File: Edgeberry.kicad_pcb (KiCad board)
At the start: 2 copper layers, 135 x 90 mm, 161 parts, among them P1 12Vin, Q1 BC547, Q2 BC547, Q3 BC547, SW1 SW_PUSH, U1 24LC256, U2 LM2596S-5.0

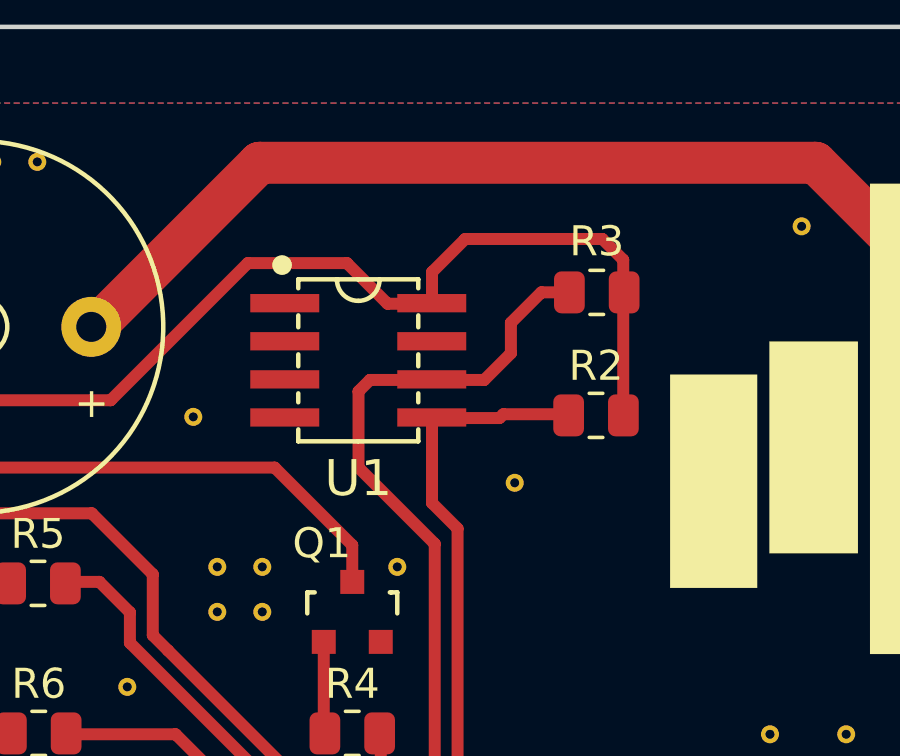
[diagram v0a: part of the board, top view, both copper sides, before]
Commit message: EEPROM write protection circuit + update version to 1.3
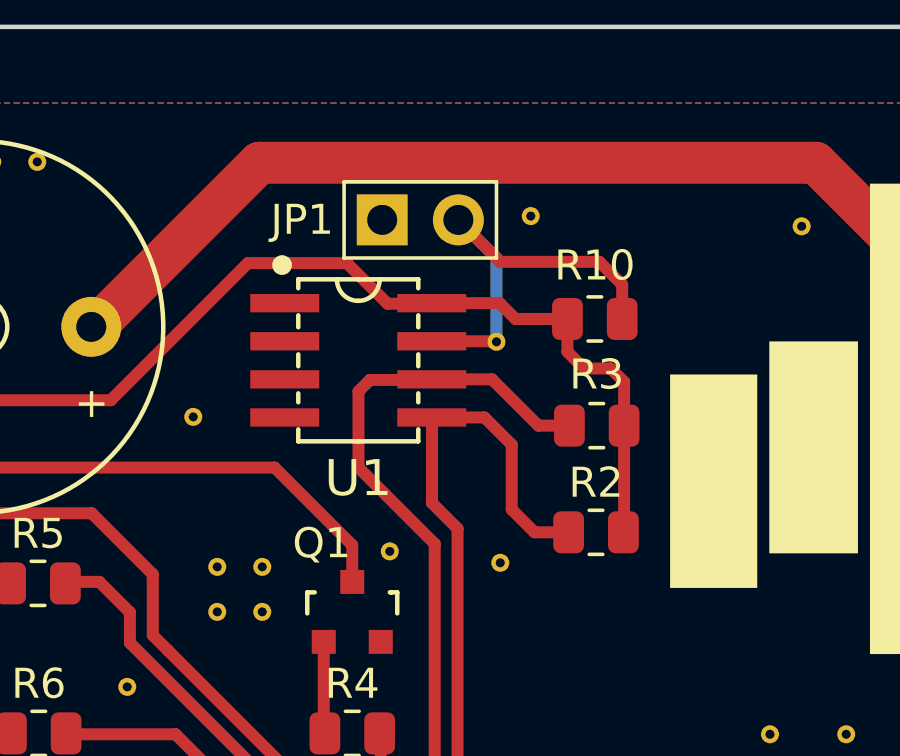
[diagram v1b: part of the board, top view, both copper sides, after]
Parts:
- added ?: , , F.Cu at (125.0, 62.3)
- added ?: , , F.Cu at (126.1, 58.1)
- added JP1: Jumper_2_Open, Connector_PinHeader_2.54mm:PinHeader_1x02_P2.54mm_Vertical, F.Cu at (121.1, 58.2)
- added R10: 10k, Resistor_SMD:R_0805_2012Metric, F.Cu at (128.2, 61.5)
- C1, C2: value 220uF -> 330uF
- moved R3 4.44 mm to (128.3, 65.1)
- moved R2 3.90 mm to (128.3, 68.6), turned to 180 degrees
- moved REF** 2.71 mm to (125.1, 69.6)
- moved REF** 0.57 mm to (121.4, 69.3)
- moved G*** 0.15 mm to (148.7, 63.3)
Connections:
- R2 pad 1: ID_SDA -> +3V3
- R2 pad 2: +3V3 -> ID_SDA
- REF** pad 1: (no net) -> GND
- U1 pad 7: GND -> WP
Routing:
- net WP: track 0.00 -> 14.3 mm
- net ID_SDA: track 29.0 -> 31.9 mm
- net ID_SCL: track 31.4 -> 30.4 mm
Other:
- board text added: "REV 1.3"
- board text added: "REV.: 1.3, Mid 2024"
- board text removed: "REV 1.2"
- board text removed: "REV.: 1.2, Mid 2024"

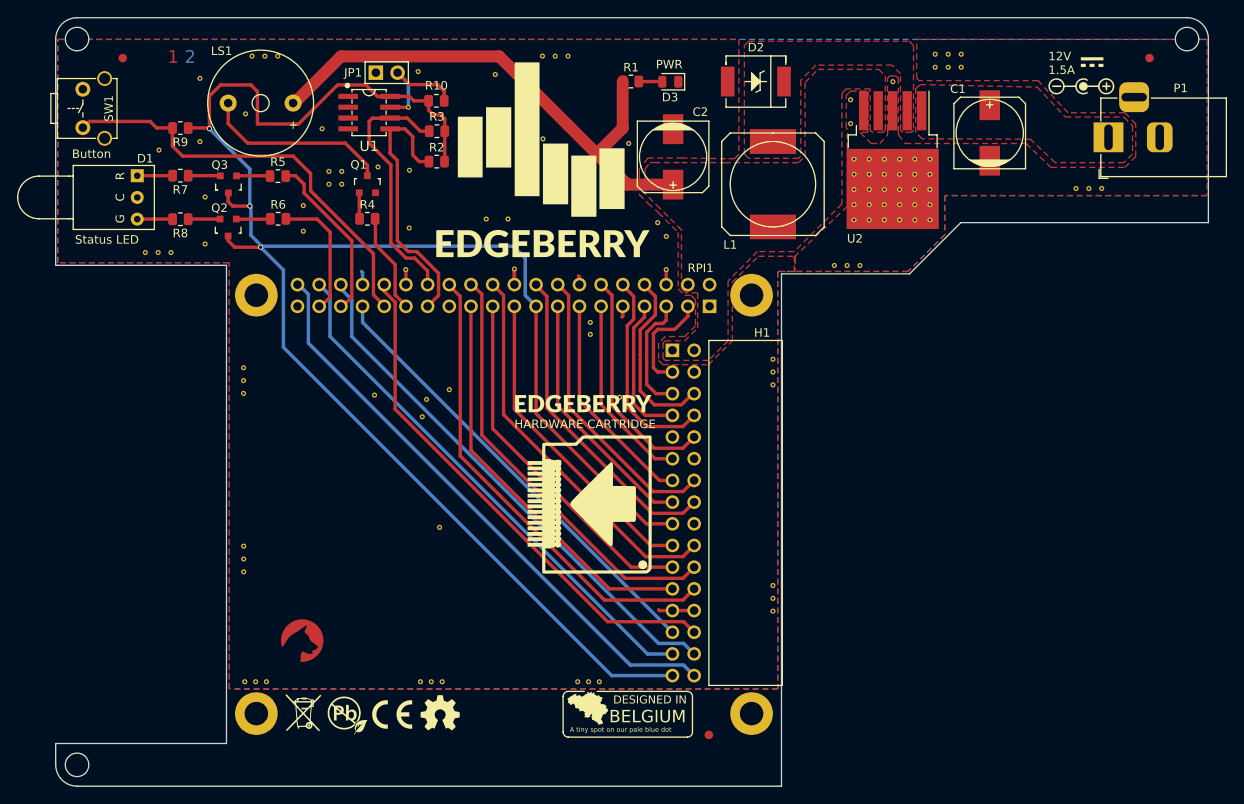
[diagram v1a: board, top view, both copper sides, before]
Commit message: Status LED on 5V instead of 3V3 + silkscreen aesthetics
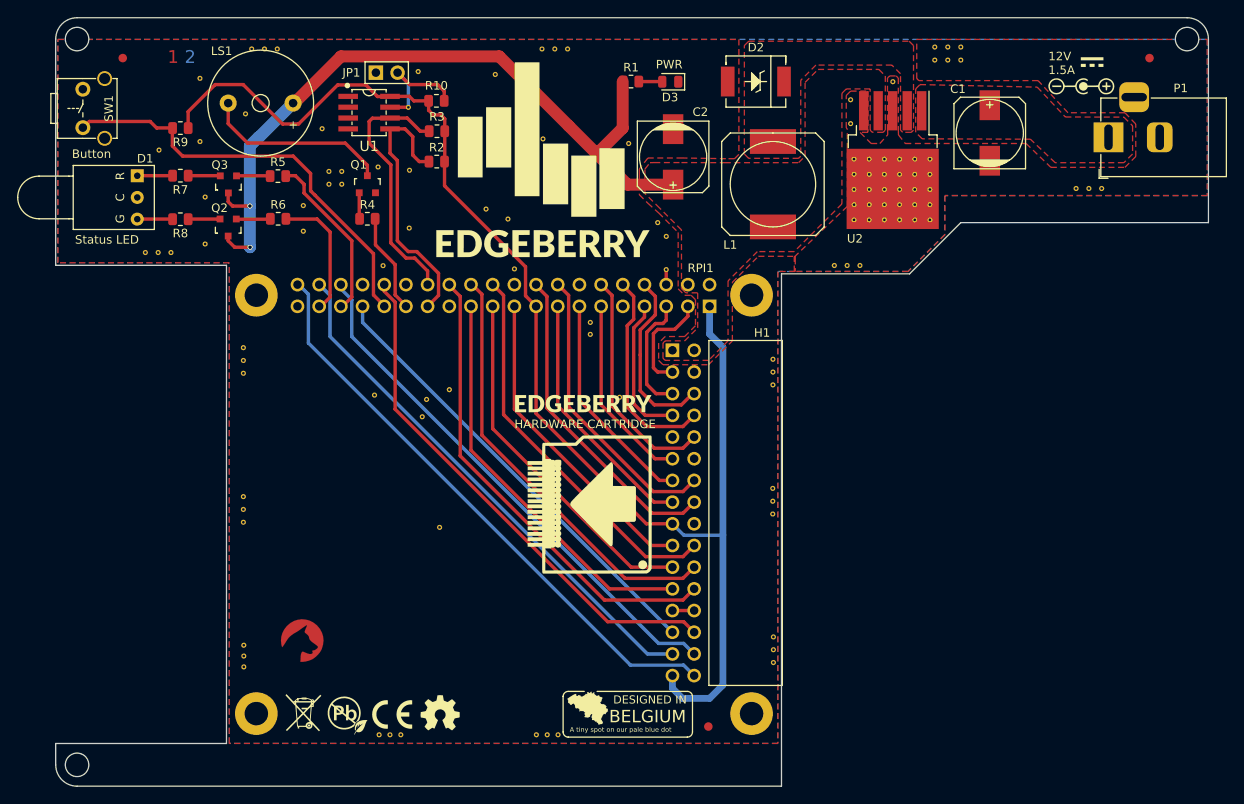
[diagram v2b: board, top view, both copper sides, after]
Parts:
- added G***: LOGO, LOGO, B.Cu at (104.8, 58.1)
- added REF**: via_0.6mm, emcosys:via_0.6mm, B.Cu at (167.7, 127.3)
- added REF**: via_0.6mm, emcosys:via_0.6mm, B.Cu at (167.7, 124.3)
- added REF**: via_0.6mm, emcosys:via_0.6mm, B.Cu at (167.7, 125.8)
- moved REF** 11.4 mm to (167.6, 108.4)
- moved REF** 11.4 mm to (167.6, 106.9)
- moved REF** 11.4 mm to (167.6, 109.9)
- moved REF** 7.87 mm to (141.2, 135.8)
- moved REF** 7.87 mm to (124.1, 135.8)
- moved REF** 7.87 mm to (122.8, 135.8)
- moved REF** 7.87 mm to (139.9, 135.8)
- moved REF** 7.87 mm to (121.5, 135.8)
- moved REF** 7.87 mm to (142.5, 135.8)
- moved REF** 5.80 mm to (105.6, 109.4)
- moved REF** 5.80 mm to (105.6, 107.9)
- moved REF** 5.80 mm to (105.6, 110.9)
- moved REF** 5.03 mm to (105.7, 125.3), turned to 0 degrees
- moved G*** 4.32 mm to (152.6, 65.2)
- moved REF** 3.31 mm to (105.7, 126.5), turned to 0 degrees
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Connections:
- Q2 pad 3: +3V3 -> +5V
- Q3 pad 3: +3V3 -> +5V
- RPI1 pad 1: unconnected-(RPI1-Pad1) -> +3V3
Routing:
- net +3V3: track 219.2 -> 160.4 mm, vias 3 -> 0
- net +5V: track 65.0 -> 91.3 mm, vias 0 -> 2
- net GND: track 16.3 -> 5.50 mm
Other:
- board text added: "Buzzer Button LED green LED red"
- board text added: "Disable EEPROM Write Protection"
- board text added: "GPIO5 GPIO6 GPIO26 GPIO19"
- board text removed: "GPIO5 - Buzzer GPIO6 - Button GPIO26 - LED green GPIO19 - LED red"
